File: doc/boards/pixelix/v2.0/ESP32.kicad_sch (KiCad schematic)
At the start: 4 parts, among them U1 ESP32-DEVKITC-32D

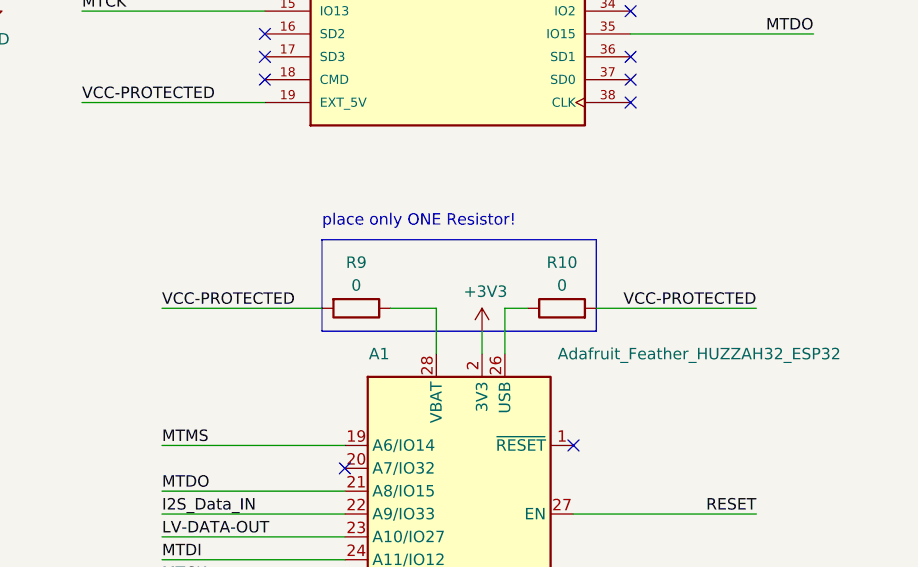
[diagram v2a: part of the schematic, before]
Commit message: Board v2.0 Schematic - remove 0 Ohm Resistors from A1 (power supply)
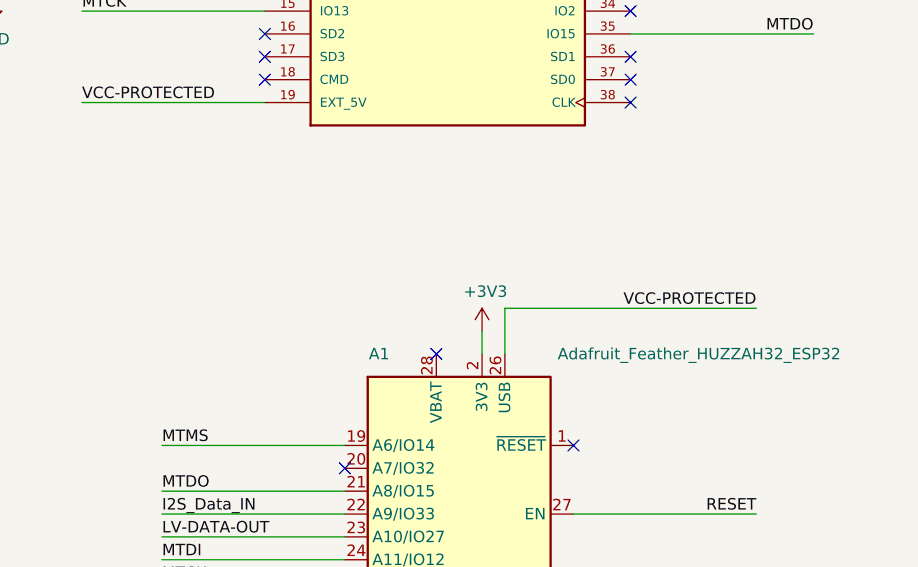
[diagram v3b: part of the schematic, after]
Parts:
- removed R10, R9: 0, Resistor_SMD:R_1206_3216Metric_Pad1.30x1.75mm_HandSolder, symbol Device:R
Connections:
- net VCC-PROTECTED: now also A1.26 (USB)
- no-connect marks 30 -> 31
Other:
- note removed: "place only ONE Resistor!"
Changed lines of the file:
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@@
   (title_block
     (title "Pixelix")
-    (date "2022-08-08")
+    (date "2022-08-12")
     (rev "2.0")
     (comment 1 "Schneider, Niklas")
@@
   (no_connect (at 180.34 43.18))
   (no_connect (at 139.7 38.1))
+  (no_connect (at 158.75 96.52))
   (no_connect (at 180.34 68.58))
   (no_connect (at 180.34 40.64))
   (no_connect (at 180.34 35.56))
-  (polyline (pts (xy 146.05 93.98) (xy 176.53 93.98))
-    (stroke (width 0) (type default) (color 0 0 0 0))
-  )
   (wire (pts (xy 57.15 60.96) (xy 36.83 60.96))
     (stroke (width 0) (type default) (color 0 0 0 0))
@@
     (stroke (width 0) (type default) (color 0 0 0 0))
   )
-  (wire (pts (xy 153.67 91.44) (xy 158.75 91.44))
-    (stroke (width 0) (type default) (color 0 0 0 0))
-  )
   (wire (pts (xy 57.15 55.88) (xy 36.83 55.88))
     (stroke (width 0) (type default) (color 0 0 0 0))
@@
     (stroke (width 0) (type default) (color 0 0 0 0))
   )
-  (wire (pts (xy 146.05 91.44) (xy 128.27 91.44))
-    (stroke (width 0) (type default) (color 0 0 0 0))
-  )
   (wire (pts (xy 166.37 91.44) (xy 166.37 96.52))
     (stroke (width 0) (type default) (color 0 0 0 0))
@@
     (stroke (width 0) (type default) (color 0 0 0 0))
   )
-  (wire (pts (xy 158.75 91.44) (xy 158.75 96.52))
-    (stroke (width 0) (type default) (color 0 0 0 0))
-  )
   (wire (pts (xy 209.55 24.13) (xy 209.55 22.86))
     (stroke (width 0) (type default) (color 0 0 0 0))
   )
-  (wire (pts (xy 176.53 91.44) (xy 194.31 91.44))
+  (wire (pts (xy 166.37 91.44) (xy 194.31 91.44))
     (stroke (width 0) (type default) (color 0 0 0 0))
   )
@@
     (stroke (width 0) (type default) (color 0 0 0 0))
   )
-  (polyline (pts (xy 146.05 83.82) (xy 146.05 93.98))
-    (stroke (width 0) (type default) (color 0 0 0 0))
-  )
   (wire (pts (xy 209.55 38.1) (xy 180.34 38.1))
     (stroke (width 0) (type default) (color 0 0 0 0))
   )
-  (wire (pts (xy 166.37 91.44) (xy 168.91 91.44))
-    (stroke (width 0) (type default) (color 0 0 0 0))
-  )
   (wire (pts (xy 134.62 22.86) (xy 139.7 22.86))
     (stroke (width 0) (type default) (color 0 0 0 0))
@@
     (stroke (width 0) (type default) (color 0 0 0 0))
   )
-  (polyline (pts (xy 146.05 83.82) (xy 176.53 83.82))
-    (stroke (width 0) (type default) (color 0 0 0 0))
-  )
   (wire (pts (xy 109.22 55.88) (xy 139.7 55.88))
     (stroke (width 0) (type default) (color 0 0 0 0))
@@
   )
   (wire (pts (xy 173.99 127) (xy 194.31 127))
-    (stroke (width 0) (type default) (color 0 0 0 0))
-  )
-  (polyline (pts (xy 176.53 93.98) (xy 176.53 83.82))
     (stroke (width 0) (type default) (color 0 0 0 0))
   )
@@
     )
   )
-  (text "place only ONE Resistor!" (at 146.05 82.55 0)
-    (effects (font (size 1.27 1.27)) (justify left bottom))
-  )
   (label "MTMS" (at 119.38 50.8 0)
     (effects (font (size 1.27 1.27)) (justify left bottom))
@@
   (label "MTDO" (at 57.15 60.96 180)
     (effects (font (size 1.27 1.27)) (justify right bottom))
-  )
-  (label "VCC-PROTECTED" (at 128.27 91.44 0)
-    (effects (font (size 1.27 1.27)) (justify left bottom))
   )
   (label "MTDO" (at 200.66 60.96 180)
@@
     (pin "1")
   )
-  (symbol (lib_id "Device:R") (at 149.86 91.44 270) (unit 1)
-    (in_bom yes) (on_board yes)
-    (property "Reference" "R9" (id 0) (at 149.86 86.36 90))
-    (property "Value" "0" (id 1) (at 149.86 88.9 90))
-    (property "Footprint" "Resistor_SMD:R_1206_3216Metric_Pad1.30x1.75mm_HandSolder" (id 2) (at 149.86 89.662 90)
-      (effects (font (size 1.27 1.27)) hide)
-    )
-    (property "Datasheet" "~" (id 3) (at 149.86 91.44 0)
-      (effects (font (size 1.27 1.27)) hide)
-    )
-    (property "Manufacturer" "-" (id 4) (at 149.86 91.44 0)
-      (effects (font (size 1.27 1.27)) hide)
-    )
-    (property "Part-No." "-" (id 5) (at 149.86 91.44 0)
-      (effects (font (size 1.27 1.27)) hide)
-    )
-    (pin "1")
-    (pin "2")
-  )
-  (symbol (lib_id "Device:R") (at 172.72 91.44 90) (unit 1)
-    (in_bom yes) (on_board yes)
-    (property "Reference" "R10" (id 0) (at 172.72 86.36 90))
-    (property "Value" "0" (id 1) (at 172.72 88.9 90))
-    (property "Footprint" "Resistor_SMD:R_1206_3216Metric_Pad1.30x1.75mm_HandSolder" (id 2) (at 172.72 93.218 90)
-      (effects (font (size 1.27 1.27)) hide)
-    )
-    (property "Datasheet" "~" (id 3) (at 172.72 91.44 0)
-      (effects (font (size 1.27 1.27)) hide)
-    )
-    (property "Manufacturer" "-" (id 4) (at 172.72 91.44 0)
-      (effects (font (size 1.27 1.27)) hide)
-    )
-    (property "Part-No." "-" (id 5) (at 172.72 91.44 0)
-      (effects (font (size 1.27 1.27)) hide)
-    )
-    (pin "1")
-    (pin "2")
-  )
 )

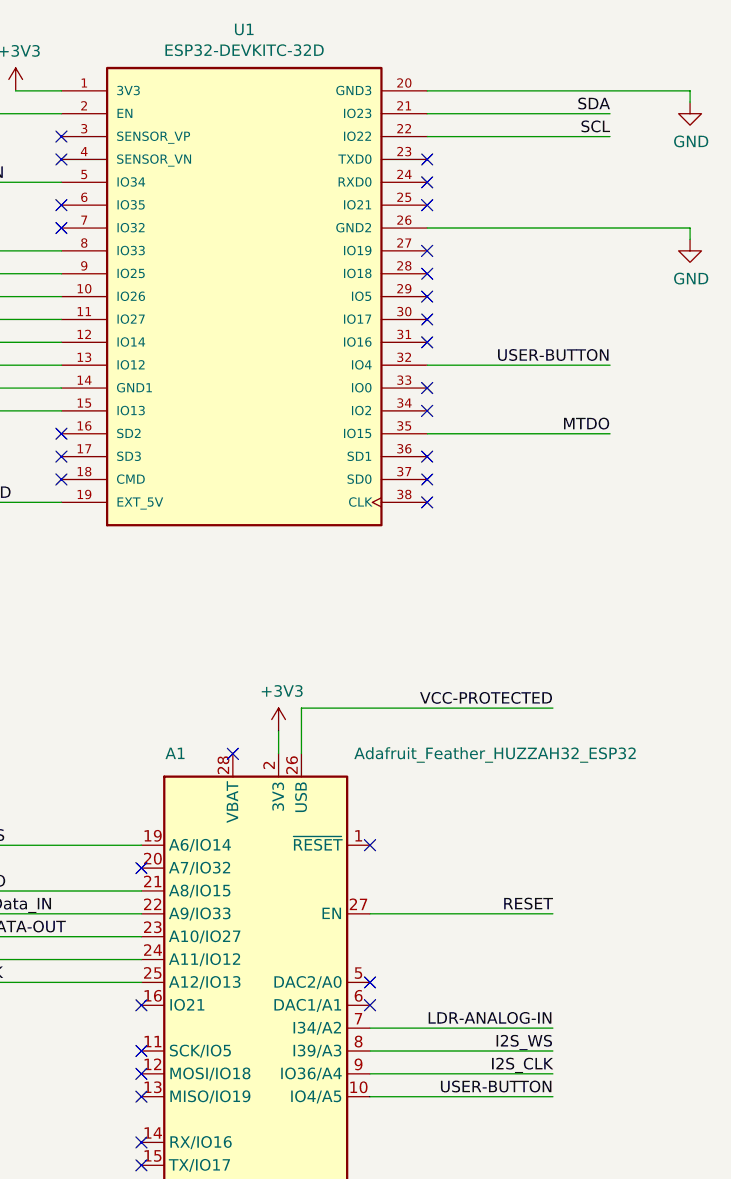
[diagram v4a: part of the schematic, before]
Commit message: Board v2.0 Schematic and PCB - DevKit: SDA from IO23 to IO21 new connected
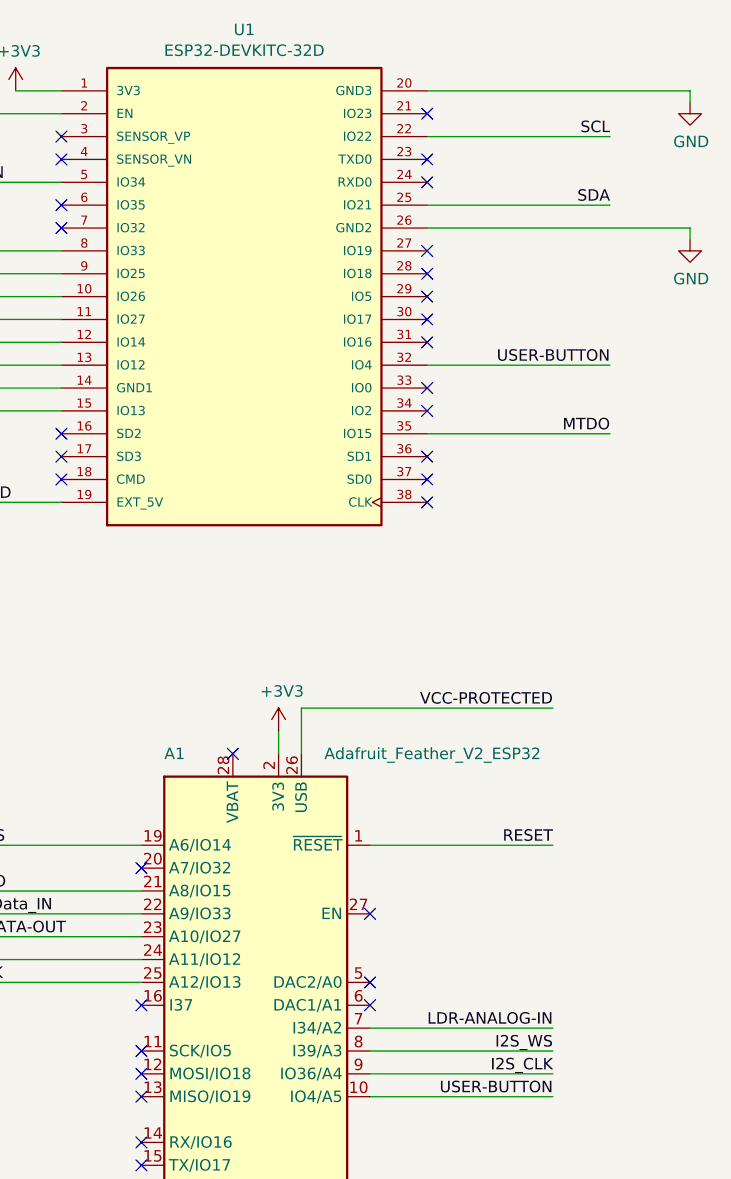
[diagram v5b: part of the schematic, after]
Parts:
- removed A1: Adafruit_Feather_HUZZAH32_ESP32, Module:Adafruit_Feather, symbol MCU_Module_new:Adafruit_Feather_HUZZAH32_ESP32
- added A1: Adafruit_Feather_V2_ESP32, footprints:Adafruit_Feather_V2_ESP32, symbol MCU_Module_Project:Adafruit_Feather_V2_ESP32
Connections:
- net +3V3: now also A1.2 (3V3)
- net GND: now also A1.4 (GND)
- net I2S_CLK: now also A1.9 (IO36/A4)
- net I2S_Data_IN: now also A1.22 (A9/IO33)
- net I2S_WS: now also A1.8 (I39/A3)
- net LDR-ANALOG-IN: now also A1.7 (I34/A2)
- net LV-DATA-OUT: now also A1.23 (A10/IO27)
- net MTCK: now also A1.25 (A12/IO13)
- net MTDI: now also A1.24 (A11/IO12)
- net MTDO: now also A1.21 (A8/IO15)
- net MTMS: now also A1.19 (A6/IO14)
- net RESET: now also A1.1 (~{RESET})
- net SCL: now also A1.18 (SCL/IO22)
- net SDA: now also U1.25 (IO21), A1.17 (SDA/IO23); no longer U1.21 (IO23)
- net USER-BUTTON: now also A1.10 (IO4/A5)
- net VCC-PROTECTED: now also A1.26 (USB)
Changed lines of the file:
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@@
   (title_block
     (title "Pixelix")
-    (date "2022-09-05")
+    (date "2022-09-12")
     (rev "2.0")
     (comment 1 "Schneider, Niklas")
@@
   (no_connect (at 139.7 66.04))
   (no_connect (at 148.59 132.08))
-  (no_connect (at 173.99 106.68))
+  (no_connect (at 173.99 114.3))
   (no_connect (at 180.34 50.8))
   (no_connect (at 180.34 63.5))
@@
   (no_connect (at 180.34 68.58))
   (no_connect (at 180.34 40.64))
-  (no_connect (at 180.34 35.56))
+  (no_connect (at 180.34 25.4))
   (wire (pts (xy 57.15 60.96) (xy 36.83 60.96))
     (stroke (width 0) (type default) (color 0 0 0 0))
@@
     (stroke (width 0) (type default) (color 0 0 0 0))
   )
-  (wire (pts (xy 200.66 25.4) (xy 180.34 25.4))
+  (wire (pts (xy 200.66 35.56) (xy 180.34 35.56))
     (stroke (width 0) (type default) (color 0 0 0 0))
   )
@@
     (stroke (width 0) (type default) (color 0 0 0 0))
   )
-  (wire (pts (xy 194.31 114.3) (xy 173.99 114.3))
+  (wire (pts (xy 194.31 106.68) (xy 173.99 106.68))
     (stroke (width 0) (type default) (color 0 0 0 0))
   )
@@
     (stroke (width 0) (type default) (color 0 0 0 0))
   )
-  (image (at 261.62 173.99) (scale 1.81836)
-    (data
-      iVBORw0KGgoAAAANSUhEUgAAAUoAAABGCAYAAACqnN3KAAAABHNCSVQICAgIfAhkiAAAAAlwSFlz
-      AAAuGAAALhgBKqonIAAAAXpJREFUeJzt3cFqwzAQRVEp///P6io7lzfGE6Sm56zN2NDmgsGDxgAA
-      AAAAAAAAAAAAAAAAaDd3P0CnNcZK18wxZvd15edbhXnzxt+kMG9snbcK8+Zsv66sMG/cmddrFZ5v
-      3ni+9v/n5nkne+1+AIDTCSVAIJQAgVACBEIJEAglQCCUAIFQAgDwzFd8Nf92+uaBzZyrefs2X2zm
-      XM2zmXPFqzdAIJQAgVACBEIJEAglQCCUAIFQAgRCCQDAM1u/ml+FzY15Y3Nj11k4Ve2bOeUbN2/c
-      lO/rzJwnujdz6vfd9fvo7UEnr94AgVACBEIJEAglQCCUAIFQAgRCCRAIJQAAz3zFeRZvp5/h4cyc
-      q3nOzPmNM3PO4dUbIBBKgEAoAQKhBAiEEiAQSoBAKAECoQQA4JlbX823n3Gz6cyc6rxuNnOu5v2F
-      M3O6r6v5b5s5J/fFqzdAIJQAgVACBEIJEAglQCCUAIFQAgRCCQAAAAAAAAAAAAAAAAB8wA+7/5tW
-      3HfTzAAAAABJRU5ErkJggg==
-    )
-  )
   (label "MTMS" (at 119.38 50.8 0)
     (effects (font (size 1.27 1.27)) (justify left bottom))
@@
     (effects (font (size 1.27 1.27)) (justify left bottom))
   )
-  (label "RESET" (at 194.31 114.3 180)
+  (label "RESET" (at 194.31 106.68 180)
     (effects (font (size 1.27 1.27)) (justify right bottom))
   )
@@
     (effects (font (size 1.27 1.27)) (justify right bottom))
   )
-  (label "SDA" (at 200.66 25.4 180)
+  (label "SDA" (at 200.66 35.56 180)
     (effects (font (size 1.27 1.27)) (justify right bottom))
   )
@@
     (pin "1")
   )
-  (symbol (lib_id "MCU_Module_new:Adafruit_Feather_HUZZAH32_ESP32") (at 161.29 127 0) (unit 1)
-    (in_bom yes) (on_board yes)
-    (property "Reference" "A1" (id 0) (at 152.4 96.52 0))
-    (property "Value" "Adafruit_Feather_HUZZAH32_ESP32" (id 1) (at 187.96 96.52 0))
-    (property "Footprint" "Module:Adafruit_Feather" (id 2) (at 163.83 161.29 0)
+  (symbol (lib_id "power:+3V3") (at 163.83 93.98 0) (unit 1)
+    (in_bom yes) (on_board yes)
+    (property "Reference" "#PWR017" (id 0) (at 163.83 97.79 0)
+      (effects (font (size 1.27 1.27)) hide)
+    )
+    (property "Value" "+3V3" (id 1) (at 164.211 89.5858 0))
+    (property "Footprint" "" (id 2) (at 163.83 93.98 0)
+      (effects (font (size 1.27 1.27)) hide)
+    )
+    (property "Datasheet" "" (id 3) (at 163.83 93.98 0)
+      (effects (font (size 1.27 1.27)) hide)
+    )
+    (pin "1")
+  )
+  (symbol (lib_id "power:GND") (at 109.22 57.15 0) (unit 1)
+    (in_bom yes) (on_board yes)
+    (property "Reference" "#PWR014" (id 0) (at 109.22 63.5 0)
+      (effects (font (size 1.27 1.27)) hide)
+    )
+    (property "Value" "GND" (id 1) (at 109.347 61.5442 0))
+    (property "Footprint" "" (id 2) (at 109.22 57.15 0)
+      (effects (font (size 1.27 1.27)) hide)
+    )
+    (property "Datasheet" "" (id 3) (at 109.22 57.15 0)
+      (effects (font (size 1.27 1.27)) hide)
+    )
+    (pin "1")
+  )
+  (symbol (lib_id "power:GND") (at 209.55 39.37 0) (unit 1)
+    (in_bom yes) (on_board yes)
+    (property "Reference" "#PWR019" (id 0) (at 209.55 45.72 0)
+      (effects (font (size 1.27 1.27)) hide)
+    )
+    (property "Value" "GND" (id 1) (at 209.677 43.7642 0))
+    (property "Footprint" "" (id 2) (at 209.55 39.37 0)
+      (effects (font (size 1.27 1.27)) hide)
+    )
+    (property "Datasheet" "" (id 3) (at 209.55 39.37 0)
+      (effects (font (size 1.27 1.27)) hide)
+    )
+    (pin "1")
+  )
+  (symbol (lib_id "power:GND") (at 209.55 24.13 0) (unit 1)
+    (in_bom yes) (on_board yes)
+    (property "Reference" "#PWR018" (id 0) (at 209.55 30.48 0)
+      (effects (font (size 1.27 1.27)) hide)
+    )
+    (property "Value" "GND" (id 1) (at 209.677 28.5242 0))
+    (property "Footprint" "" (id 2) (at 209.55 24.13 0)
+      (effects (font (size 1.27 1.27)) hide)
+    )
+    (property "Datasheet" "" (id 3) (at 209.55 24.13 0)
+      (effects (font (size 1.27 1.27)) hide)
+    )
+    (pin "1")
+  )
+  (symbol (lib_id "power:GND") (at 161.29 163.83 0) (unit 1)
+    (in_bom yes) (on_board yes)
+    (property "Reference" "#PWR016" (id 0) (at 161.29 170.18 0)
+      (effects (font (size 1.27 1.27)) hide)
+    )
+    (property "Value" "GND" (id 1) (at 161.417 168.2242 0))
+    (property "Footprint" "" (id 2) (at 161.29 163.83 0)
+      (effects (font (size 1.27 1.27)) hide)
+    )
+    (property "Datasheet" "" (id 3) (at 161.29 163.83 0)
+      (effects (font (size 1.27 1.27)) hide)
+    )
+    (pin "1")
+  )
+  (symbol (lib_id "MCU_Module_Project:Adafruit_Feather_V2_ESP32") (at 161.29 127 0) (unit 1)
+    (in_bom yes) (on_board yes)
+    (property "Reference" "A1" (id 0) (at 151.13 96.52 0)
+      (effects (font (size 1.27 1.27)) (justify left))
+    )
+    (property "Value" "Adafruit_Feather_V2_ESP32" (id 1) (at 168.91 96.52 0)
+      (effects (font (size 1.27 1.27)) (justify left))
+    )
+    (property "Footprint" "footprints:Adafruit_Feather_V2_ESP32" (id 2) (at 163.83 161.29 0)
       (effects (font (size 1.27 1.27)) (justify left) hide)
     )
-    (property "Datasheet" "https://cdn-learn.adafruit.com/downloads/pdf/adafruit-huzzah32-esp32-feather.pdf" (id 3) (at 161.29 157.48 0)
-      (effects (font (size 1.27 1.27)) hide)
-    )
-    (property "Manufacturer" "Adafruit Feather" (id 4) (at 161.29 127 0)
-      (effects (font (size 1.27 1.27)) hide)
-    )
-    (property "Part-No." "HUZZAH32" (id 5) (at 161.29 127 0)
+    (property "Datasheet" "https://cdn-learn.adafruit.com/downloads/pdf/adafruit-esp32-feather-v2.pdf" (id 3) (at 161.29 157.48 0)
+      (effects (font (size 1.27 1.27)) hide)
+    )
+    (property "Manufacturer" "Adafruit" (id 4) (at 161.29 127 0)
+      (effects (font (size 1.27 1.27)) hide)
+    )
+    (property "Part-No." "Feather V2" (id 5) (at 161.29 127 0)
       (effects (font (size 1.27 1.27)) hide)
     )
@@
     (pin "9")
   )
-  (symbol (lib_id "power:+3V3") (at 163.83 93.98 0) (unit 1)
-    (in_bom yes) (on_board yes)
-    (property "Reference" "#PWR017" (id 0) (at 163.83 97.79 0)
-      (effects (font (size 1.27 1.27)) hide)
-    )
-    (property "Value" "+3V3" (id 1) (at 164.211 89.5858 0))
-    (property "Footprint" "" (id 2) (at 163.83 93.98 0)
-      (effects (font (size 1.27 1.27)) hide)
-    )
-    (property "Datasheet" "" (id 3) (at 163.83 93.98 0)
-      (effects (font (size 1.27 1.27)) hide)
-    )
-    (pin "1")
-  )
-  (symbol (lib_id "power:GND") (at 109.22 57.15 0) (unit 1)
-    (in_bom yes) (on_board yes)
-    (property "Reference" "#PWR014" (id 0) (at 109.22 63.5 0)
-      (effects (font (size 1.27 1.27)) hide)
-    )
-    (property "Value" "GND" (id 1) (at 109.347 61.5442 0))
-    (property "Footprint" "" (id 2) (at 109.22 57.15 0)
-      (effects (font (size 1.27 1.27)) hide)
-    )
-    (property "Datasheet" "" (id 3) (at 109.22 57.15 0)
-      (effects (font (size 1.27 1.27)) hide)
-    )
-    (pin "1")
-  )
-  (symbol (lib_id "power:GND") (at 209.55 39.37 0) (unit 1)
-    (in_bom yes) (on_board yes)
-    (property "Reference" "#PWR019" (id 0) (at 209.55 45.72 0)
-      (effects (font (size 1.27 1.27)) hide)
-    )
-    (property "Value" "GND" (id 1) (at 209.677 43.7642 0))
-    (property "Footprint" "" (id 2) (at 209.55 39.37 0)
-      (effects (font (size 1.27 1.27)) hide)
-    )
-    (property "Datasheet" "" (id 3) (at 209.55 39.37 0)
-      (effects (font (size 1.27 1.27)) hide)
-    )
-    (pin "1")
-  )
-  (symbol (lib_id "power:GND") (at 209.55 24.13 0) (unit 1)
-    (in_bom yes) (on_board yes)
-    (property "Reference" "#PWR018" (id 0) (at 209.55 30.48 0)
-      (effects (font (size 1.27 1.27)) hide)
-    )
-    (property "Value" "GND" (id 1) (at 209.677 28.5242 0))
-    (property "Footprint" "" (id 2) (at 209.55 24.13 0)
-      (effects (font (size 1.27 1.27)) hide)
-    )
-    (property "Datasheet" "" (id 3) (at 209.55 24.13 0)
-      (effects (font (size 1.27 1.27)) hide)
-    )
-    (pin "1")
-  )
-  (symbol (lib_id "power:GND") (at 161.29 163.83 0) (unit 1)
-    (in_bom yes) (on_board yes)
-    (property "Reference" "#PWR016" (id 0) (at 161.29 170.18 0)
-      (effects (font (size 1.27 1.27)) hide)
-    )
-    (property "Value" "GND" (id 1) (at 161.417 168.2242 0))
-    (property "Footprint" "" (id 2) (at 161.29 163.83 0)
-      (effects (font (size 1.27 1.27)) hide)
-    )
-    (property "Datasheet" "" (id 3) (at 161.29 163.83 0)
-      (effects (font (size 1.27 1.27)) hide)
-    )
-    (pin "1")
-  )
 )
